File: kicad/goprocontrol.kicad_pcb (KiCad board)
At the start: 2 copper layers, 58.9 x 58.9 mm, 37 parts, among them P1 CONN_01X06, Q1 MMBT3904, Q2 MMBT3904, Q3 MMBT3906, Q4 MMBT3906, Q5 IRLML6344, SW1 Reset, SW2 Prog, U1 NE555, U2 ESP-01v090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

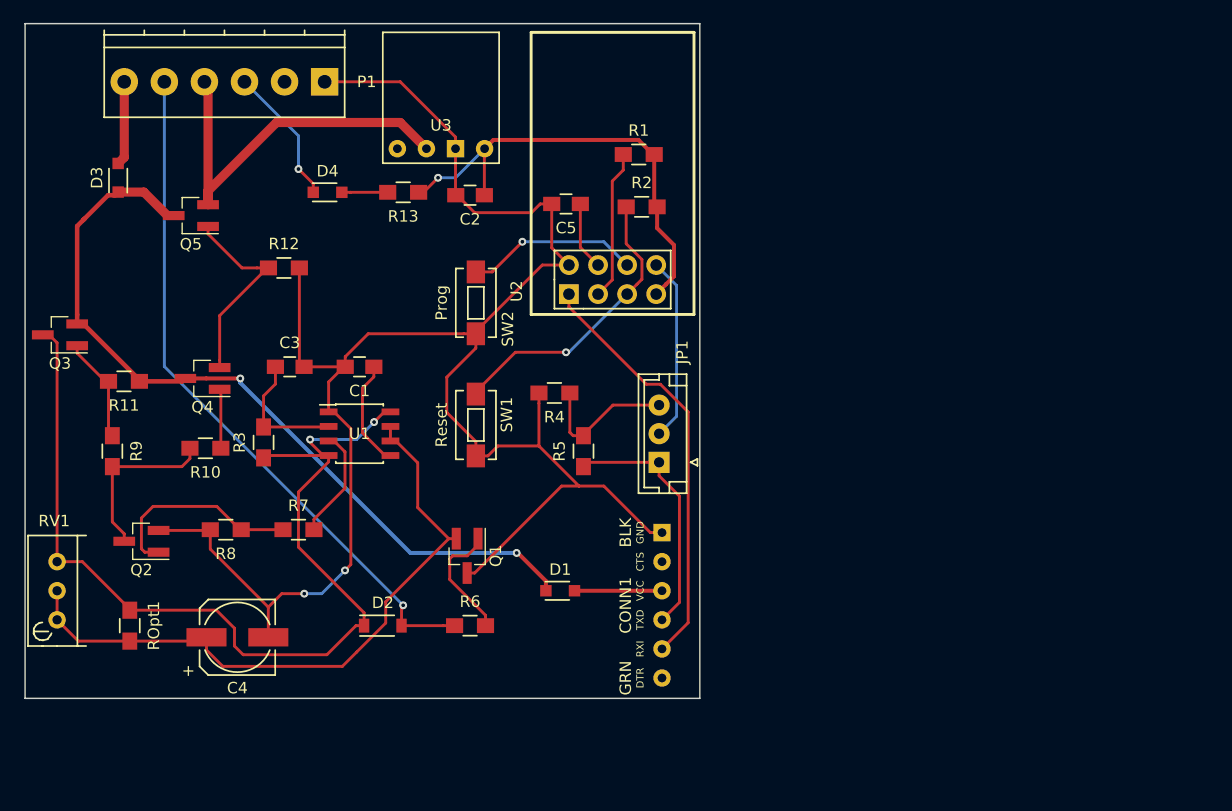
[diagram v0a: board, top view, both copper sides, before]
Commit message: Design new v2.0 board
Still ESP8266 based
Add delaytimer v1.1 circuit for power control
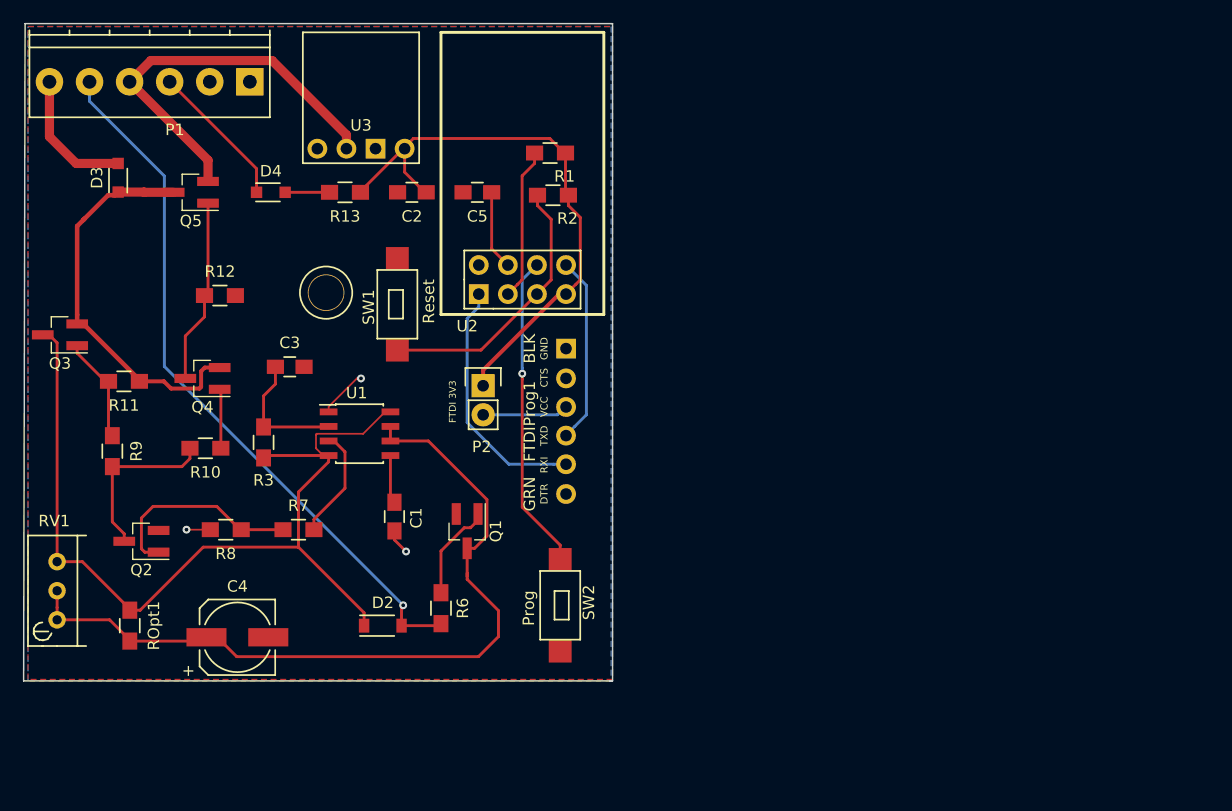
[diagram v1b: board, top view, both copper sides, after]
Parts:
- removed CONN1: FTDI, synfinatic:FTDIHeader
- removed D1: B5817WS, Diodes_SMD:SOD-323_HandSoldering
- removed JP1: Jumper_NC_Dual, Connectors_JST:JST_EH_B03B-EH-A_03x2.50mm_Straight
- removed R4: 10k, Resistors_SMD:R_0805_HandSoldering
- removed R5: 22k, Resistors_SMD:R_0805_HandSoldering
- added ?: 1pin, Connectors:1pin, F.Cu at (131.2, 95.9)
- added FTDIProg1: FTDI, synfinatic:FTDIHeader, F.Cu at (152.1, 107.1)
- added P2: CONN_01X02, Pin_Headers:Pin_Header_Straight_1x02, F.Cu at (144.9, 104.0)
- SW1, SW2: footprint Buttons_Switches_SMD:SW_SPST_EVQPE1 -> synfinatic:SPST-SMD-6x3.5
- moved SW2 27.4 mm to (151.6, 123.2), turned to 0 degrees
- moved C1 13.4 mm to (137.2, 115.4), turned to 270 degrees
- moved SW1 12.6 mm to (137.4, 96.9), turned to 180 degrees
- moved U2 7.87 mm to (144.5, 96.0)
- moved R2 7.81 mm to (151.0, 87.4)
- moved C5 7.81 mm to (144.4, 87.1)
- moved R1 7.75 mm to (150.7, 83.7)
- moved U3 6.99 mm to (129.2, 80.8)
- moved P1 6.53 mm to (124.5, 77.5)
- moved R12 6.09 mm to (121.9, 96.1)
- moved C2 5.09 mm to (138.7, 87.1)
- moved R13 5.08 mm to (132.8, 87.1)
- moved D4 4.95 mm to (126.4, 87.1)
- moved R6 2.96 mm to (141.2, 123.4), turned to 90 degrees
- moved Q1 2.16 mm to (143.5, 116.7)
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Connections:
- P1 pad 2: (no net) -> Net-(P1-Pad2)
- Q1 pad 2: Net-(C4-Pad1) -> GND
- Q1 pad 3: GND -> Net-(C4-Pad1)
- Q4 pad 2: Net-(Q4-Pad2) -> +12V
- Q4 pad 3: +12V -> Net-(Q4-Pad3)
- Q5 pad 1: Net-(Q4-Pad2) -> Net-(Q4-Pad3)
- R12 pad 1: Net-(Q4-Pad2) -> Net-(Q4-Pad3)
- U3 pad 1: (no net) -> Net-(U3-Pad1)
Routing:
- net GND: track 164.2 -> 8.60 mm, vias 2 -> 3
- net +12V: track 70.8 -> 34.8 mm, vias 2 -> 0
- net Net-(CONN1-Pad3): track 21.9 -> 0.00 mm
- net Net-(Q4-Pad2): track 17.7 -> 0.00 mm
- net Net-(Q4-Pad3): track 0.00 -> 16.7 mm
- net TXD: track 37.0 -> 21.8 mm
- net Net-(JP1-Pad3): track 12.5 -> 0.00 mm
- net Net-(SW2-Pad1): track 15.1 -> 27.6 mm
- net Net-(C4-Pad1): track 57.9 -> 69.8 mm
- net +3V3: track 40.6 -> 50.1 mm, vias 1 -> 0
- net Net-(CONN1-Pad4): track 7.64 -> 0.00 mm
- net Net-(FTDIProg1-Pad4): track 0.00 -> 7.55 mm
- net VCC: track 87.3 -> 80.4 mm, vias 2 -> 0
- net Net-(C1-Pad1): track 9.45 -> 4.70 mm
- net Net-(D3-Pad2): track 7.35 -> 11.8 mm
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- added copper zone on B.Cu, net GND
- added copper zone on F.Cu, net GND
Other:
- board size 58.9 x 58.9 mm -> 51.4 x 57.4 mm
- board text added: "FTDI 3V3"
- board text added: "GoProControl v2.0 https://synfin.net/goprocontrol"
- board text added: "S/N:"

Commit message: GoProControl v2.1 ordered
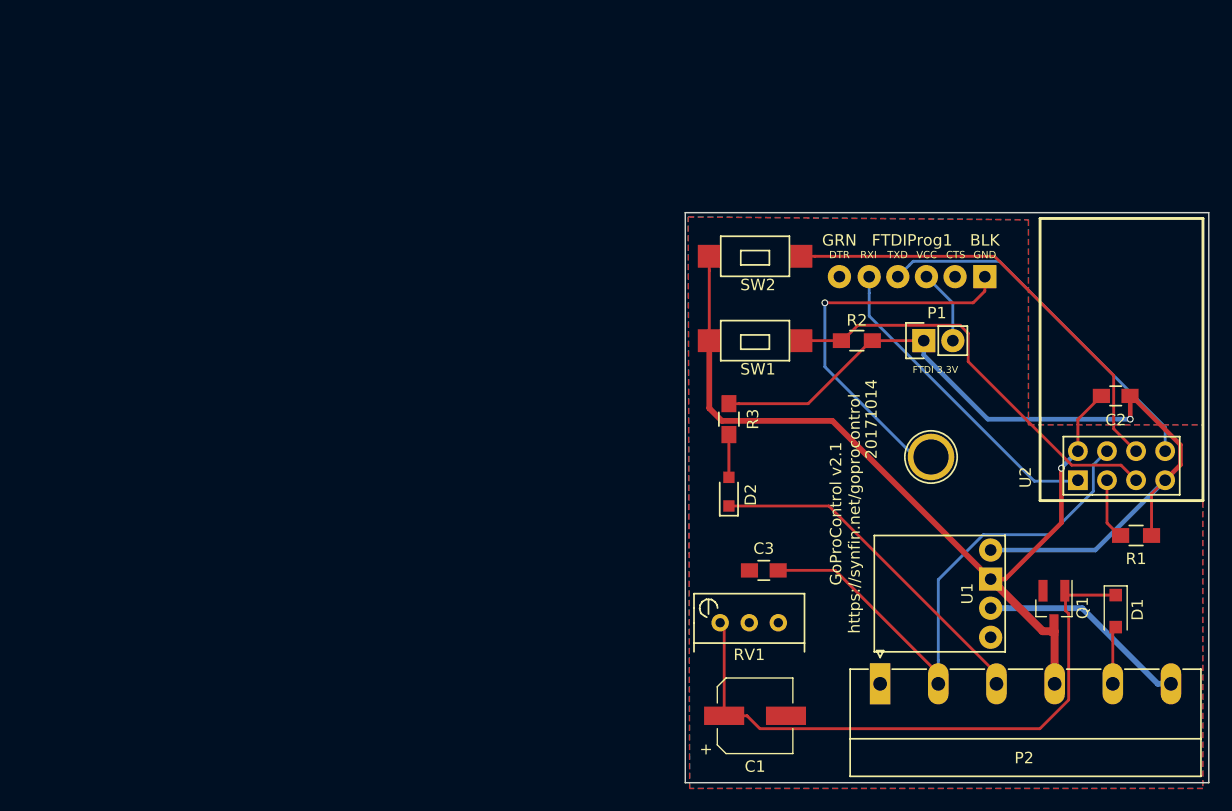
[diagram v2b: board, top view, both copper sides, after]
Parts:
- removed ?: 1pin, Connectors:1pin
- removed C4: 100uf, Capacitors_SMD:c_elec_6.3x7.7
- removed C5: .01uf, Capacitors_SMD:C_0805_HandSoldering
- removed D3, D4: B5817WS, Diodes_SMD:SOD-323_HandSoldering
- removed Q2: MMBT3904, TO_SOT_Packages_SMD:SOT-23_Handsoldering
- removed Q3, Q4: MMBT3906, TO_SOT_Packages_SMD:SOT-23_Handsoldering
- removed Q5: IRLML6344, TO_SOT_Packages_SMD:SOT-23_Handsoldering
- removed R10, R11, R6, R8: 2.2k, Resistors_SMD:R_0805_HandSoldering
- removed R12, R13: 1k, Resistors_SMD:R_0805_HandSoldering
- removed R7, R9: 10k, Resistors_SMD:R_0805_HandSoldering
- removed ROpt1: 100k, Resistors_SMD:R_0805_HandSoldering
- removed U3: D24V5F3, synfinatic:D24V5Fx
- added D1: D_Zener, Diodes_SMD:D_SOD-123F, F.Cu at (200.2, 123.7)
- added REF**: 1pin, Connectors:1pin, F.Cu at (184.0, 110.2)
- C1: value 0.1uf -> 100uF; footprint Capacitors_SMD:C_0805_HandSoldering -> Capacitors_SMD:CP_Elec_6.3x7.7
- C3: value 0.1uf -> .01uf
- D2: value 1n4148 -> B5817WS; footprint Diodes_SMD:SOD-123 -> Diodes_SMD:SOD-323_HandSoldering
- P1: value CONN_01X06 -> CONN_01X02; footprint Connectors_Terminal_Blocks:TerminalBlock_Pheonix_PT-3.5mm_6pol -> Pin_Headers:Pin_Header_Straight_1x02
- P2: value CONN_01X02 -> CONN_01X06; footprint Pin_Headers:Pin_Header_Straight_1x02 -> Connectors_Phoenix:PhoenixContact_MC-G_06x5.08mm_Angled
- Q1: value MMBT3904 -> IRLML6344
- R3: value 100k -> 1k
- RV1: value 500k -> POT
- U1: value NE555 -> D24V5F3; footprint Housings_SOIC:SOIC-8_3.9x4.9mm_Pitch1.27mm -> synfinatic:D24V5Fx
- moved C2 64.0 mm to (200.2, 104.9)
- moved P1 63.0 mm to (183.4, 100.1), turned to 90 degrees
- moved R1 61.1 mm to (201.9, 117.1)
- moved RV1 57.9 mm to (165.6, 124.7), turned to 270 degrees
- moved U1 55.9 mm to (186.7, 127.3), turned to 90 degrees
- moved U2 54.8 mm to (196.8, 112.3)
- moved Q1 51.7 mm to (194.8, 123.4)
- moved C3 45.1 mm to (169.4, 120.1), turned to 180 degrees
- moved P2 43.4 mm to (179.6, 130.0)
- moved R3 40.7 mm to (166.4, 106.9), turned to 270 degrees
- moved C1 36.0 mm to (168.7, 132.8), turned to 0 degrees
- moved SW2 34.9 mm to (168.7, 92.7), turned to 270 degrees
- moved FTDIProg1 32.8 mm to (182.4, 94.5), turned to 0 degrees
- moved D2 32.4 mm to (166.4, 113.3), turned to 90 degrees
- moved SW1 31.4 mm to (168.7, 100.1), turned to 270 degrees
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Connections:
- C2 pad 2: GND -> SwitchedGndOut
- C3 pad 1: Net-(C3-Pad1) -> GPIO2
- D2 pad 1: VCC -> LoggerTrigger
- D2 pad 2: Switched12V -> Net-(D2-Pad2)
- P1 pad 1: GND -> +3V3
- P1 pad 2: Net-(P1-Pad2) -> Net-(FTDIProg1-Pad4)
- P2 pad 1: +3V3 -> GND
- P2 pad 2: Net-(FTDIProg1-Pad4) -> GPIO2
- Q1 pad 1: Net-(Q1-Pad1) -> Net-(C1-Pad1)
- Q1 pad 3: Net-(C4-Pad1) -> SwitchedGndOut
- R3 pad 1: VCC -> +3V3
- R3 pad 2: Net-(C3-Pad1) -> Net-(D2-Pad2)
- RV1 pad 1: Net-(C4-Pad1) -> Net-(C1-Pad1)
- RV1 pad 2: Net-(C4-Pad1) -> GND
- RV1 pad 3: VCC -> Net-(RV1-Pad3)
- SW1 pad 2: GND -> SwitchedGndOut
- SW2 pad 2: GND -> SwitchedGndOut
- U1 pad 1: GND -> Net-(U1-Pad1)
- U1 pad 2: Net-(C3-Pad1) -> +12V
- U1 pad 3: Net-(R7-Pad2) -> SwitchedGndOut
- U1 pad 4: VCC -> +3V3
- U2 pad 2: GND -> SwitchedGndOut
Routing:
- net VCC: track 80.4 -> 0.00 mm
- net SwitchedGndOut: track 0.00 -> 76.8 mm, vias 0 -> 1
- net Net-(C4-Pad1): track 69.8 -> 0.00 mm
- net Switched12V: track 62.4 -> 5.06 mm, vias 1 -> 0
- net Net-(C1-Pad1): track 4.70 -> 53.4 mm
- net GPIO2: track 7.12 -> 48.5 mm
- net 12VOut: track 35.0 -> 0.00 mm
- net GND: track 8.60 -> 34.5 mm, vias 3 -> 1
- net +3V3: track 50.1 -> 75.9 mm, vias 0 -> 1
- net Net-(Q2-Pad1): track 17.9 -> 0.00 mm
- net LoggerTrigger: track 12.8 -> 30.3 mm
- net Net-(Q4-Pad3): track 16.7 -> 0.00 mm
- net +12V: track 34.8 -> 18.5 mm
- net RXD: track 16.3 -> 32.0 mm
- net Net-(Q2-Pad3): track 14.9 -> 0.00 mm
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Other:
- board size 51.4 x 57.4 mm -> 45.7 x 49.8 mm
- net class +12V added: clearance 0.2, trace_width 0.504, via_dia 0.6, via_drill 0.4
- net class 0.2mm removed
- net class 12VPower removed
- net class Default: clearance 0.254 -> 0.2; trace_width 0.254 -> 0.25; via_dia 0.6858 -> 0.6; via_drill 0.3302 -> 0.4
- net class Minimal removed
- net class SwitchedGnd added: clearance 0.2, trace_width 0.7, via_dia 0.6, via_drill 0.4
- rule trace_clearance: 0.254 -> 0.2
- rule trace_min: 0.1524 -> 0.2
- rule via_min_drill: 0.3302 -> 0.3
- rule via_min_size: 0.6858 -> 0.4
- board text added: "20171014"
- board text added: "FTDI 3.3V"
- board text added: "GPIO2"
- board text added: "GoProControl v2.1 https://synfin.net/goprocontrol"
- board text added: "Switched GND"
- board text added: "Trigger"
- board text removed: "12VOut 2A"
- board text removed: "FTDI 3V3"
- board text removed: "GoProControl v2.0 https://synfin.net/goprocontrol"
- board text removed: "Logger Trigger"
- board text removed: "S/N:"

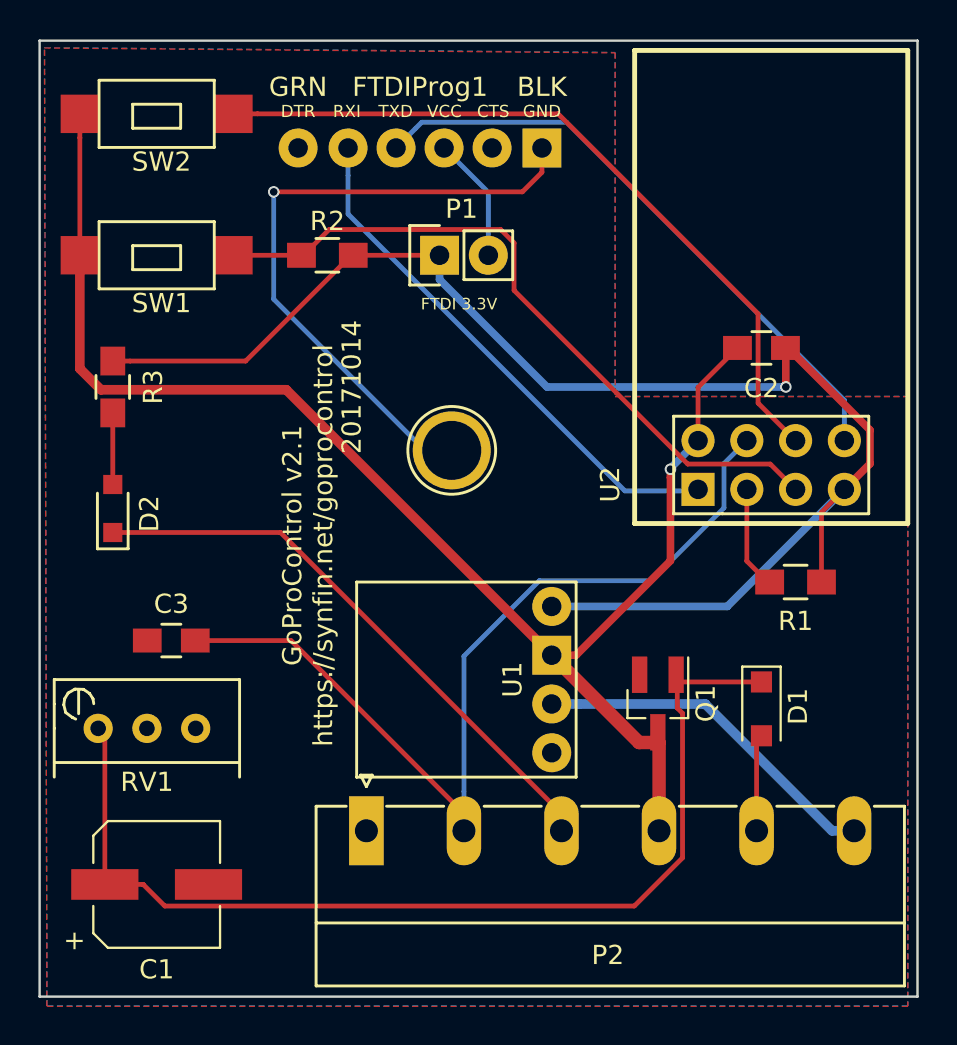
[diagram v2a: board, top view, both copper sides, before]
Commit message: Rev board to v2.2
- Switch to using ESP12E
- Switch to using OptoIsolator + ESP power off detection
- Using Pot to control power off delay
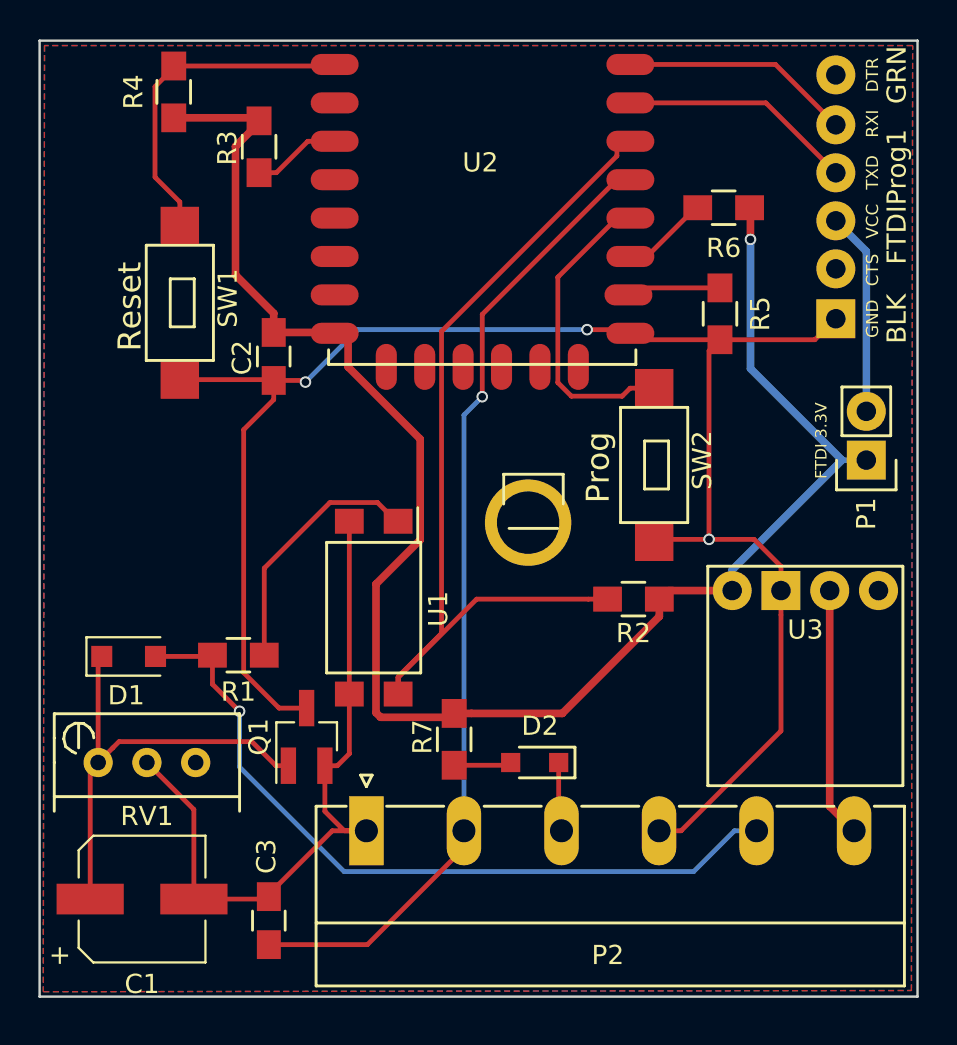
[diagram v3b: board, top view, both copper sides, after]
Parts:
- removed REF**: 1pin, Connectors:1pin
- added ?: Pin_Header_Straight_1x01, Pin_Headers:Pin_Header_Straight_1x01, F.Cu at (188.3, 113.0)
- added R4: 1K, Resistors_SMD:R_0805_HandSoldering, F.Cu at (169.5, 91.6)
- added R5: 4.7K, Resistors_SMD:R_0805_HandSoldering, F.Cu at (198.0, 103.1)
- added R6: 1K, Resistors_SMD:R_0805_HandSoldering, F.Cu at (198.2, 97.6)
- added R7: 1k, Resistors_SMD:R_0805_HandSoldering, F.Cu at (184.2, 125.3)
- added U3: D24V5F3, synfinatic:D24V5Fx, F.Cu at (207.5, 120.1)
- D1: value D_Zener -> 10VZener
- R1: value 1k -> 560
- R2: value 1k -> 10K
- R3: value 1k -> 1K
- U1: value D24V5F3 -> LTV-814; footprint synfinatic:D24V5Fx -> Opto-Devices:Optocoupler_SMD_LTV-817S
- U2: value ESP-01v090 -> ESP-12E; footprint ESP8266:ESP-01 -> synfinatic:ESP-12E-SMD
- moved D1 33.1 mm to (167.2, 121.0), turned to 0 degrees
- moved SW2 31.7 mm to (194.6, 111.0), turned to 0 degrees
- moved R1 29.3 mm to (172.9, 120.9), turned to 180 degrees
- moved U2 28.7 mm to (178.6, 90.1), turned to 0 degrees
- moved D2 25.6 mm to (188.3, 126.5), turned to 180 degrees
- moved C2 25.4 mm to (174.8, 105.3), turned to 270 degrees
- moved P1 24.7 mm to (205.6, 110.7), turned to 180 degrees
- moved R2 24.0 mm to (193.5, 118.0), turned to 180 degrees
- moved FTDIProg1 21.8 mm to (204.0, 97.0), turned to 270 degrees
- moved Q1 18.4 mm to (176.5, 125.2), turned to 90 degrees
- moved C3 15.4 mm to (174.5, 134.7), turned to 90 degrees
- moved R3 14.6 mm to (174.0, 94.4)
- moved U1 11.1 mm to (180.0, 118.4), turned to 270 degrees
- moved SW1 2.75 mm to (169.9, 102.6), turned to 0 degrees
- moved RV1 1.78 mm to (165.6, 126.5)
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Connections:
- C2 pad 2: SwitchedGndOut -> SwitchedGnd
- C3 pad 1: GPIO2 -> GPIO4
- FTDIProg1 pad 1: Net-(FTDIProg1-Pad1) -> (no net)
- FTDIProg1 pad 5: Net-(FTDIProg1-Pad5) -> (no net)
- FTDIProg1 pad 6: GND -> SwitchedGnd
- P2 pad 2: GPIO2 -> GPIO4
- P2 pad 4: SwitchedGndOut -> SwitchedGnd
- Q1 pad 3: SwitchedGndOut -> SwitchedGnd
- R1 pad 2: +3V3 -> Switched12V
- R2 pad 1: Net-(R2-Pad1) -> +3V3
- R2 pad 2: +3V3 -> GPIO5
- R3 pad 2: Net-(D2-Pad2) -> Net-(R3-Pad2)
- RV1 pad 3: Net-(RV1-Pad3) -> (no net)
- SW1 pad 1: Net-(R2-Pad1) -> Net-(R4-Pad2)
- SW1 pad 2: SwitchedGndOut -> SwitchedGnd
- SW2 pad 2: SwitchedGndOut -> SwitchedGnd
- U1 pad 1: Net-(U1-Pad1) -> Net-(R1-Pad1)
- U1 pad 2: +12V -> GND
- U1 pad 3: SwitchedGndOut -> GND
- U1 pad 4: +3V3 -> GPIO5
- U2 pad 1: TXD -> Net-(R4-Pad2)
- U2 pad 2: SwitchedGndOut -> (no net)
- U2 pad 3: Net-(R1-Pad1) -> Net-(R3-Pad2)
- U2 pad 4: GPIO2 -> (no net)
- U2 pad 5: Net-(R2-Pad1) -> (no net)
- U2 pad 6: Net-(SW2-Pad1) -> (no net)
- U2 pad 7: +3V3 -> (no net)
- U2 pad 8: RXD -> +3V3
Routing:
- net SwitchedGnd: track 0.00 -> 91.0 mm, vias 0 -> 3
- net SwitchedGndOut: track 76.8 -> 0.00 mm, vias 1 -> 0
- net GPIO4: track 0.00 -> 50.4 mm, vias 0 -> 1
- net GPIO2: track 48.5 -> 0.00 mm
- net GPIO5: track 0.00 -> 47.1 mm
- net Net-(R2-Pad1): track 36.9 -> 0.00 mm
- net Switched12V: track 5.06 -> 39.5 mm, vias 0 -> 1
- net Net-(C1-Pad1): track 53.4 -> 23.8 mm
- net LoggerTrigger: track 30.3 -> 3.62 mm
- net Net-(SW2-Pad1): track 39.0 -> 15.3 mm
- net RXD: track 32.0 -> 12.9 mm
- net Net-(R4-Pad2): track 0.00 -> 18.4 mm
- net +3V3: track 75.9 -> 91.8 mm
- net TXD: track 27.7 -> 12.7 mm
- net Net-(R1-Pad1): track 5.38 -> 13.3 mm
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- added copper zone on B.Cu, net +3V3
- added copper zone on F.Cu, net SwitchedGnd
- removed copper zone on B.Cu, net GND
- removed copper zone on F.Cu, net GND
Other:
- net class +12V: trace_width 0.504 -> 0.4
- net class +3V3 added: clearance 0.2, trace_width 0.4, via_dia 0.6, via_drill 0.4
- net class SwitchedGnd: trace_width 0.7 -> 0.25
- board text added: "20180218"
- board text added: "GPIO4"
- board text added: "GoProControl v2.2 https://synfin.net/goprocontrol"
- board text added: "Prog"
- board text added: "Reset"
- board text removed: "20171014"
- board text removed: "GPIO2"
- board text removed: "GoProControl v2.1 https://synfin.net/goprocontrol"
